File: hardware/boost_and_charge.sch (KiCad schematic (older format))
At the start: 36 parts, among them J1 Conn_01x02_Female, SW5 SW_Push, U4 MCP73871, U5 TPS61090

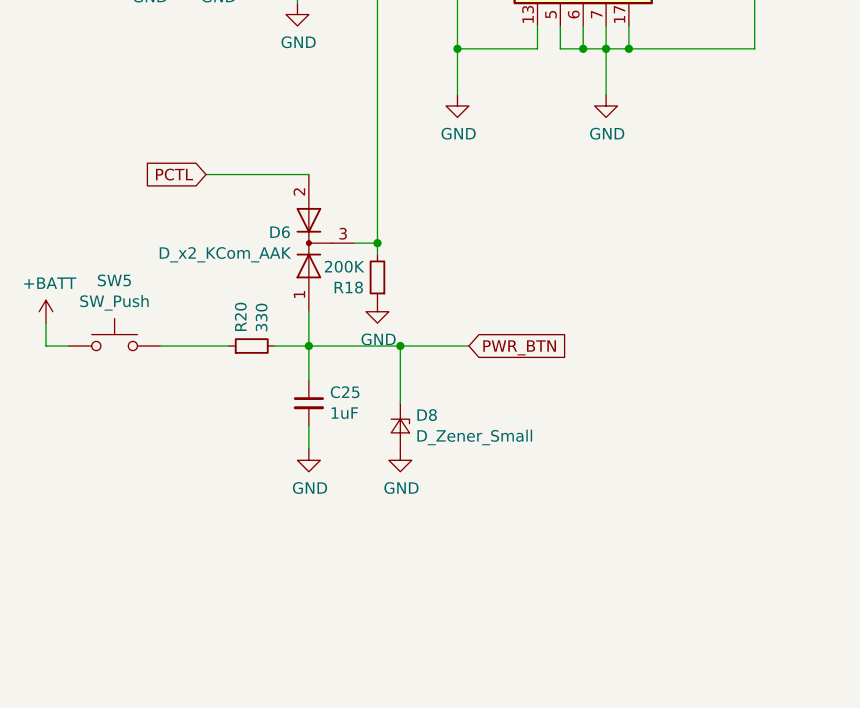
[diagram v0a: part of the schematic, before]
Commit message: fixing incorrect PWR_BUTTON net on schematic and PCB
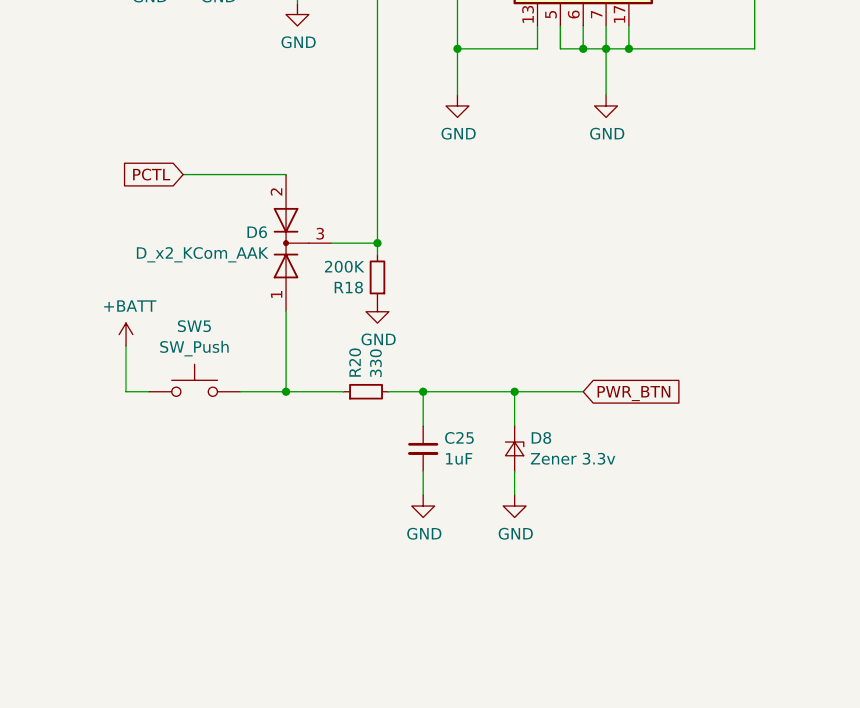
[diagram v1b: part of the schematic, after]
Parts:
- D8: value D_Zener_Small -> Zener 3.3v
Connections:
- net PWR_BTN: no longer D6.1 (A)
- net at R20.1, SW5.1: now also D6.1 (A)
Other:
- moved on the sheet: C25, D6, D8, R20, SW5
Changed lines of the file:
@@
 EESchema Schematic File Version 4
-LIBS:Open Op-cache
+LIBS:teensy_beats-cache
 EELAYER 26 0
 EELAYER END
@@
 L Switch:SW_Push SW5
 U 1 1 5B985C32
-P 1200 5000
-F 0 "SW5" H 1200 5285 50  0000 C CNN
-F 1 "SW_Push" H 1200 5194 50  0000 C CNN
-F 2 "Buttons_Switches_THT:SW_Tactile_SKHH_Angled" H 1200 5200 50  0001 C CNN
-F 3 "" H 1200 5200 50  0001 C CNN
-	1    1200 5000
+P 1550 5200
+F 0 "SW5" H 1550 5485 50  0000 C CNN
+F 1 "SW_Push" H 1550 5394 50  0000 C CNN
+F 2 "Buttons_Switches_THT:SW_Tactile_SKHH_Angled" H 1550 5400 50  0001 C CNN
+F 3 "" H 1550 5400 50  0001 C CNN
+	1    1550 5200
 	-1   0    0    -1
 $EndComp
@@
 L Device:D_x2_KCom_AAK D6
 U 1 1 5B985FD7
-P 2050 4550
-F 0 "D6" V 2096 4629 50  0000 L CNN
-F 1 "D_x2_KCom_AAK" V 2005 4629 50  0000 L CNN
-F 2 "digikey-footprints:SOT-23-3" H 2050 4550 50  0001 C CNN
-F 3 "~" H 2050 4550 50  0001 C CNN
-	1    2050 4550
+P 1950 4550
+F 0 "D6" V 1996 4629 50  0000 L CNN
+F 1 "D_x2_KCom_AAK" V 1905 4629 50  0000 L CNN
+F 2 "digikey-footprints:SOT-23-3" H 1950 4550 50  0001 C CNN
+F 3 "~" H 1950 4550 50  0001 C CNN
+	1    1950 4550
 	0    -1   -1   0
 $EndComp
 Wire Wire Line
-	2350 4550 2250 4550
-Wire Wire Line
 	2350 2900 2350 4550
 Wire Wire Line
-	2050 4250 1600 4250
-Text GLabel 1600 4250 0    50   Input ~ 0
+	1950 4250 1500 4250
+Text GLabel 1500 4250 0    50   Input ~ 0
 PCTL
 $Comp
 L power:+BATT #PWR0118
 U 1 1 5B99939F
-P 900 4900
-F 0 "#PWR0118" H 900 4750 50  0001 C CNN
-F 1 "+BATT" H 915 5073 50  0000 C CNN
-F 2 "" H 900 4900 50  0001 C CNN
-F 3 "" H 900 4900 50  0001 C CNN
-	1    900  4900
-	1    0    0    -1
-$EndComp
-Wire Wire Line
-	1000 5000 900  5000
-Wire Wire Line
-	900  5000 900  4900
+P 1250 5000
+F 0 "#PWR0118" H 1250 4850 50  0001 C CNN
+F 1 "+BATT" H 1265 5173 50  0000 C CNN
+F 2 "" H 1250 5000 50  0001 C CNN
+F 3 "" H 1250 5000 50  0001 C CNN
+	1    1250 5000
+	1    0    0    -1
+$EndComp
+Wire Wire Line
+	1350 5200 1250 5200
 $Comp
 L Device:R_Small R20
 U 1 1 5B99F151
-P 1800 5000
-F 0 "R20" H 1859 5046 50  0000 L CNN
-F 1 "330" H 1859 4955 50  0000 L CNN
-F 2 "Resistors_SMD:R_0805" H 1800 5000 50  0001 C CNN
-F 3 "~" H 1800 5000 50  0001 C CNN
-	1    1800 5000
+P 2300 5200
+F 0 "R20" H 2359 5246 50  0000 L CNN
+F 1 "330" H 2359 5155 50  0000 L CNN
+F 2 "Resistors_SMD:R_0805" H 2300 5200 50  0001 C CNN
+F 3 "~" H 2300 5200 50  0001 C CNN
+	1    2300 5200
 	0    -1   -1   0
 $EndComp
 Wire Wire Line
-	2050 5000 2050 4850
-Wire Wire Line
-	1900 5000 2050 5000
+	2400 5200 2550 5200
 $Comp
 L Device:R_Small R18
@@
 L Device:C_Small C25
 U 1 1 5B9B7E1B
-P 2050 5250
-F 0 "C25" H 2142 5296 50  0000 L CNN
-F 1 "1uF" H 2142 5205 50  0000 L CNN
-F 2 "Capacitors_SMD:C_0805" H 2050 5250 50  0001 C CNN
-F 3 "~" H 2050 5250 50  0001 C CNN
-	1    2050 5250
-	1    0    0    -1
-$EndComp
-Connection ~ 2050 5000
-Wire Wire Line
-	2050 5350 2050 5450
+P 2550 5450
+F 0 "C25" H 2642 5496 50  0000 L CNN
+F 1 "1uF" H 2642 5405 50  0000 L CNN
+F 2 "Capacitors_SMD:C_0805" H 2550 5450 50  0001 C CNN
+F 3 "~" H 2550 5450 50  0001 C CNN
+	1    2550 5450
+	1    0    0    -1
+$EndComp
+Connection ~ 2550 5200
+Wire Wire Line
+	2550 5550 2550 5650
 $Comp
 L power:GND #PWR0120
 U 1 1 5B9C12A0
-P 2050 5450
-F 0 "#PWR0120" H 2050 5200 50  0001 C CNN
-F 1 "GND" H 2055 5277 50  0000 C CNN
-F 2 "" H 2050 5450 50  0001 C CNN
-F 3 "" H 2050 5450 50  0001 C CNN
-	1    2050 5450
-	1    0    0    -1
-$EndComp
-Wire Wire Line
-	2450 5000 2750 5000
-Text GLabel 2750 5000 2    50   Input ~ 0
+P 2550 5650
+F 0 "#PWR0120" H 2550 5400 50  0001 C CNN
+F 1 "GND" H 2555 5477 50  0000 C CNN
+F 2 "" H 2550 5650 50  0001 C CNN
+F 3 "" H 2550 5650 50  0001 C CNN
+	1    2550 5650
+	1    0    0    -1
+$EndComp
+Text GLabel 3250 5200 2    50   Input ~ 0
 PWR_BTN
 Wire Wire Line
 	2350 4550 2350 4600
 Connection ~ 2350 4550
-Wire Wire Line
-	1400 5000 1700 5000
-Wire Wire Line
-	2050 5000 2450 5000
-Wire Wire Line
-	2450 5000 2450 5250
 $Comp
 L Device:D_Zener_Small D8
 U 1 1 5B99D094
-P 2450 5350
-F 0 "D8" V 2404 5418 50  0000 L CNN
-F 1 "D_Zener_Small" V 2495 5418 50  0000 L CNN
-F 2 "Diodes_SMD:D_SOD-323" V 2450 5350 50  0001 C CNN
-F 3 "~" V 2450 5350 50  0001 C CNN
-	1    2450 5350
+P 2950 5450
+F 0 "D8" V 2904 5518 50  0000 L CNN
+F 1 "Zener 3.3v" V 2995 5518 50  0000 L CNN
+F 2 "Diodes_SMD:D_SOD-323" V 2950 5450 50  0001 C CNN
+F 3 "~" V 2950 5450 50  0001 C CNN
+	1    2950 5450
 	0    1    1    0
 $EndComp
@@
 L power:GND #PWR0121
 U 1 1 5B99D120
-P 2450 5450
-F 0 "#PWR0121" H 2450 5200 50  0001 C CNN
-F 1 "GND" H 2455 5277 50  0000 C CNN
-F 2 "" H 2450 5450 50  0001 C CNN
-F 3 "" H 2450 5450 50  0001 C CNN
-	1    2450 5450
-	1    0    0    -1
-$EndComp
-Wire Wire Line
-	2050 5000 2050 5150
-Connection ~ 2450 5000
+P 2950 5650
+F 0 "#PWR0121" H 2950 5400 50  0001 C CNN
+F 1 "GND" H 2955 5477 50  0000 C CNN
+F 2 "" H 2950 5650 50  0001 C CNN
+F 3 "" H 2950 5650 50  0001 C CNN
+	1    2950 5650
+	1    0    0    -1
+$EndComp
+Wire Wire Line
+	2550 5200 2550 5350
 Text GLabel 9900 2600 2    50   Input ~ 0
 VLIPO
@@
 	0    1    1    0
 $EndComp
+Wire Wire Line
+	2150 4550 2350 4550
+Wire Wire Line
+	1750 5200 1950 5200
+Wire Wire Line
+	1250 5000 1250 5200
+Wire Wire Line
+	1950 4850 1950 5200
+Connection ~ 1950 5200
+Wire Wire Line
+	1950 5200 2200 5200
+Wire Wire Line
+	2550 5200 2950 5200
+Wire Wire Line
+	2950 5550 2950 5650
+Wire Wire Line
+	2950 5350 2950 5200
+Connection ~ 2950 5200
+Wire Wire Line
+	2950 5200 3250 5200
 $EndSCHEMATC

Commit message: changed pin mapping to add pg signal, added enable jumper for development. adding updated gerbers.
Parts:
- added J4: Conn_01x02_Male, Pin_Headers:Pin_Header_Straight_1x02_Pitch1.27mm, symbol Connector:Conn_01x02_Male
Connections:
- net +BATT: now also J4.2 (Pin_2)
- net at D6.3 (K), R18.2, U5.11 (EN): now also J4.1 (Pin_1)
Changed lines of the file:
@@
 Wire Wire Line
 	2950 5200 3250 5200
+$Comp
+L Connector:Conn_01x02_Male J4
+U 1 1 5BC7B36B
+P 3250 4550
+F 0 "J4" H 3356 4728 50  0000 C CNN
+F 1 "Conn_01x02_Male" H 3356 4637 50  0000 C CNN
+F 2 "Pin_Headers:Pin_Header_Straight_1x02_Pitch1.27mm" H 3250 4550 50  0001 C CNN
+F 3 "~" H 3250 4550 50  0001 C CNN
+	1    3250 4550
+	-1   0    0    1
+$EndComp
+Wire Wire Line
+	2350 4550 3050 4550
+$Comp
+L power:+BATT #PWR0156
+U 1 1 5BC8AFCC
+P 2900 4350
+F 0 "#PWR0156" H 2900 4200 50  0001 C CNN
+F 1 "+BATT" H 2915 4523 50  0000 C CNN
+F 2 "" H 2900 4350 50  0001 C CNN
+F 3 "" H 2900 4350 50  0001 C CNN
+	1    2900 4350
+	1    0    0    -1
+$EndComp
+Wire Wire Line
+	2900 4350 2900 4450
+Wire Wire Line
+	2900 4450 3050 4450
 $EndSCHEMATC
